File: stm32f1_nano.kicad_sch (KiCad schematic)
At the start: 50 parts, among them J1 Analog, J2 Digital, J3 TYPE-C-31-M-12, J4 Conn_ST_STDC14, J5 DEBUG, Q1 AO3401A, U1 STM32F103C8T6, U2 W25Q128JVSIQ, U3 AMS1117-3.3, U4 XC6206P332MR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

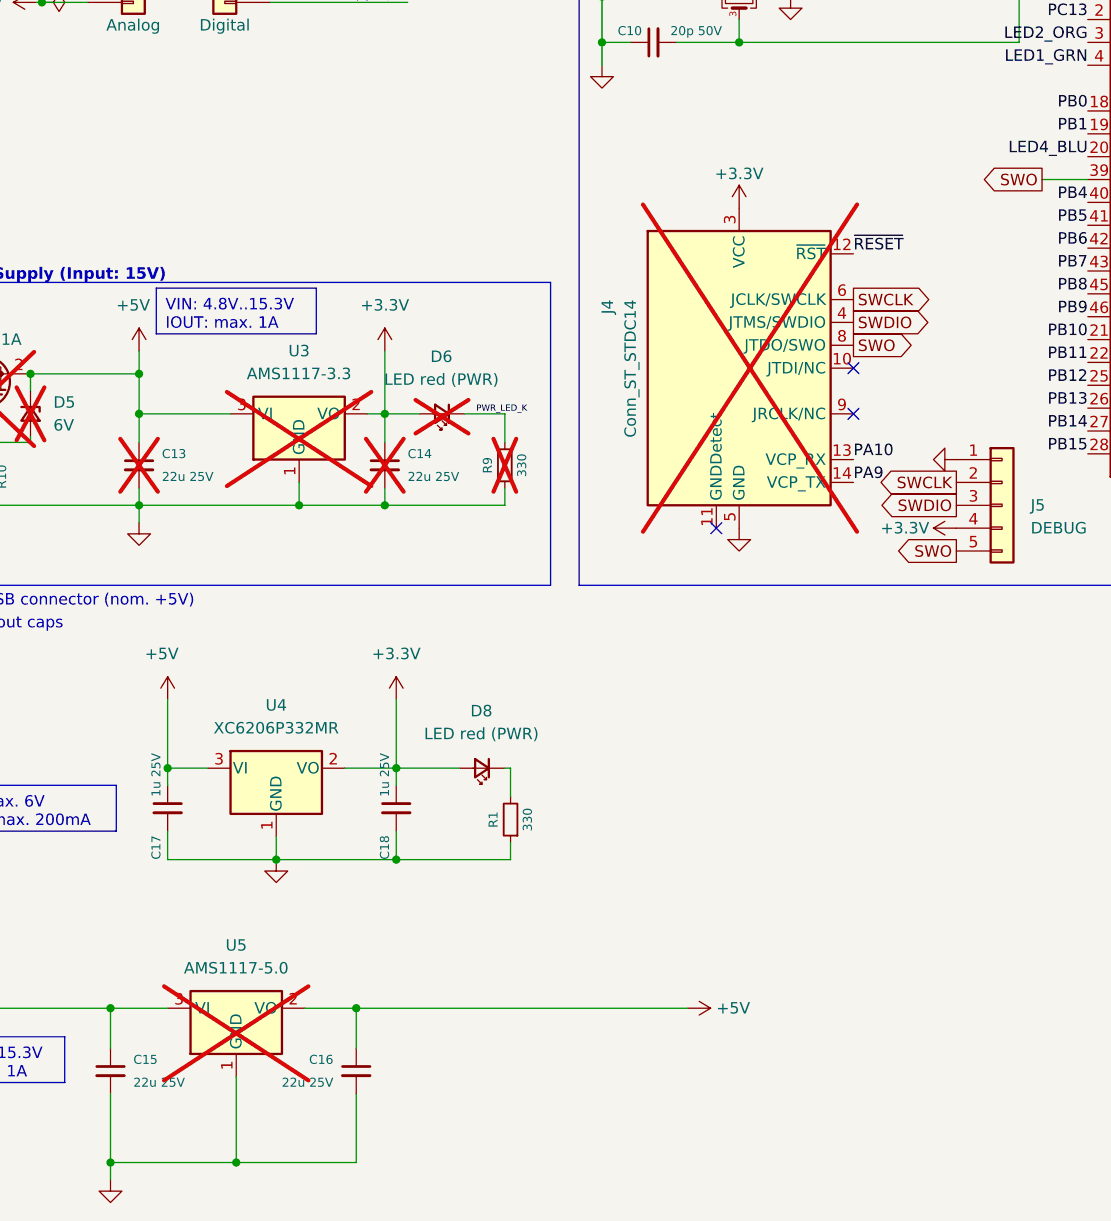
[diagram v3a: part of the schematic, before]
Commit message: #11 Use new central library KiCad-Lib
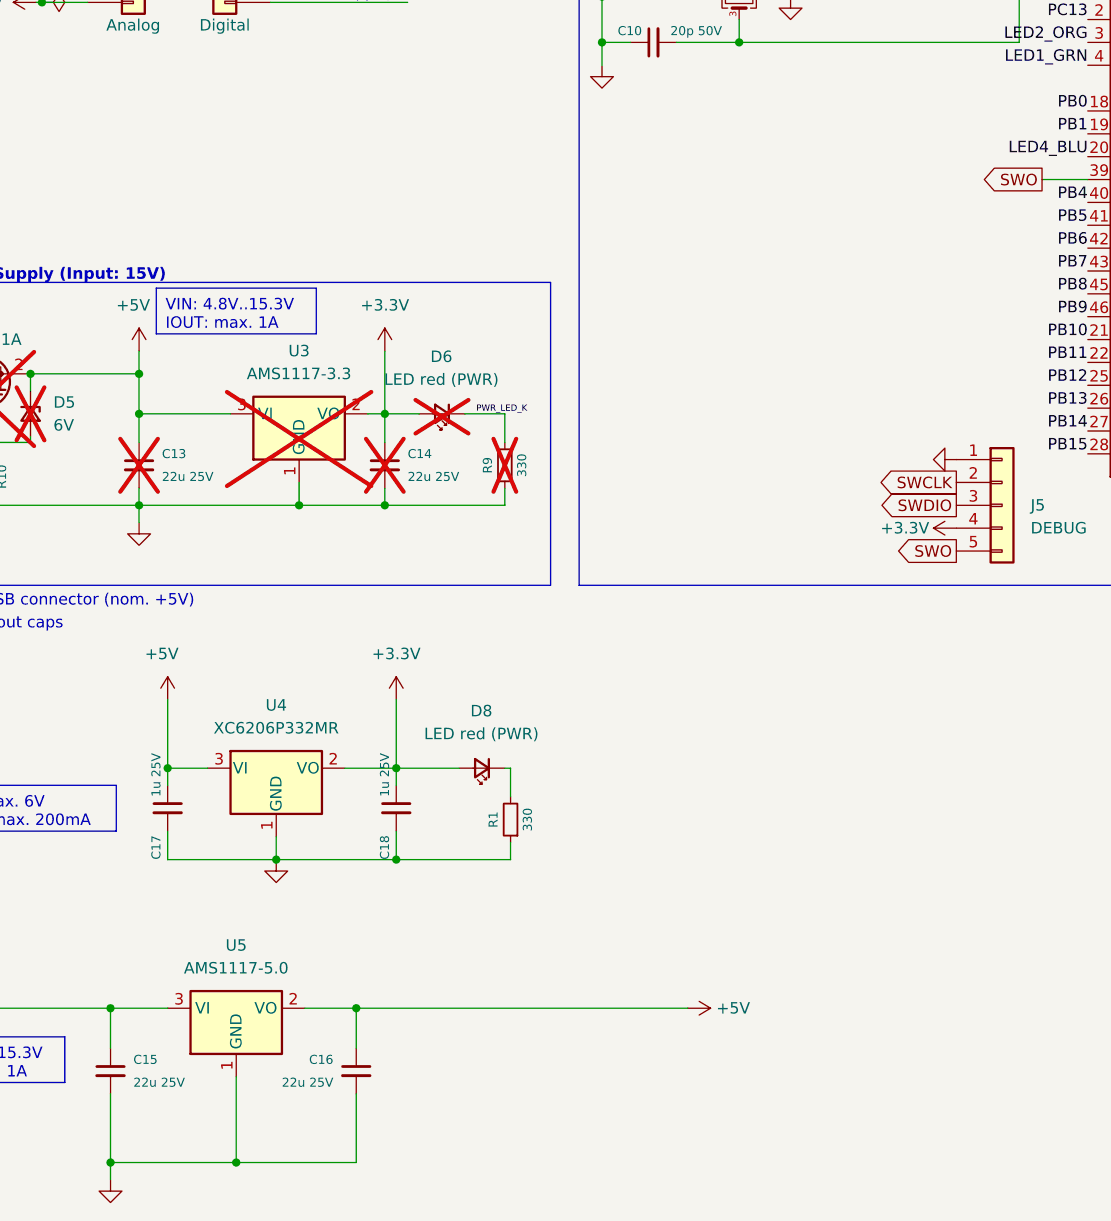
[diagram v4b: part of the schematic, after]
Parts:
- removed J4: Conn_ST_STDC14, Project_Library:Samtec_FTSH-107-XX-YYY-DV-K-A, symbol Connector:Conn_ST_STDC14
- U5: now fitted
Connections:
- no-connect marks 7 -> 4
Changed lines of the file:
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@@
   )
   (no_connect (at 35.56 31.75))
-  (no_connect (at 120.65 102.87))
-  (no_connect (at 120.65 107.95))
   (no_connect (at 236.22 111.76))
   (no_connect (at 55.88 57.15))
-  (no_connect (at 105.41 120.65))
   (no_connect (at 236.22 109.22))
   (wire (pts (xy 55.88 59.69) (xy 71.12 59.69))
@@
     (effects (font (size 1.27 1.27)) (justify right bottom))
   )
-  (label "PA10" (at 120.65 113.03 0) (fields_autoplaced)
-    (effects (font (size 1.27 1.27)) (justify left bottom))
-  )
   (label "PB14" (at 146.685 109.855 180) (fields_autoplaced)
     (effects (font (size 1.27 1.27)) (justify right bottom))
@@
     (effects (font (size 1.27 1.27)) (justify left bottom))
   )
-  (label "PA9" (at 120.65 115.57 0) (fields_autoplaced)
-    (effects (font (size 1.27 1.27)) (justify left bottom))
-  )
   (label "SPI1_MOSI" (at 179.705 92.075 0) (fields_autoplaced)
     (effects (font (size 1.27 1.27)) (justify left bottom))
@@
     (effects (font (size 1.27 1.27)) (justify left bottom))
   )
-  (label "~{RESET}" (at 120.65 90.17 0) (fields_autoplaced)
-    (effects (font (size 1.27 1.27)) (justify left bottom))
-  )
   (global_label "SWO" (shape output) (at 132.08 123.19 180) (fields_autoplaced)
     (effects (font (size 1.27 1.27)) (justify right))
@@
     )
   )
-  (global_label "SWDIO" (shape output) (at 120.65 97.79 0) (fields_autoplaced)
-    (effects (font (size 1.27 1.27)) (justify left))
-    (property "Intersheetrefs" "${INTERSHEET_REFS}" (at 128.9293 97.8694 0)
-      (effects (font (size 1.27 1.27)) (justify left) hide)
-    )
-  )
   (global_label "SWO" (shape output) (at 141.605 81.915 180) (fields_autoplaced)
     (effects (font (size 1.27 1.27)) (justify right))
@@
     )
   )
-  (global_label "SWO" (shape output) (at 120.65 100.33 0) (fields_autoplaced)
-    (effects (font (size 1.27 1.27)) (justify left))
-    (property "Intersheetrefs" "${INTERSHEET_REFS}" (at 127.0545 100.2506 0)
-      (effects (font (size 1.27 1.27)) (justify left) hide)
-    )
-  )
-  (global_label "SWCLK" (shape output) (at 120.65 95.25 0) (fields_autoplaced)
-    (effects (font (size 1.27 1.27)) (justify left))
-    (property "Intersheetrefs" "${INTERSHEET_REFS}" (at 129.2921 95.3294 0)
-      (effects (font (size 1.27 1.27)) (justify left) hide)
-    )
-  )
   (symbol (lib_id "Connector_Generic:Conn_01x15") (at 40.64 44.45 0) (unit 1)
     (in_bom no) (on_board yes) (dnp no)
@@
   )
   (symbol (lib_id "Device:C_Small") (at 201.93 80.01 180) (unit 1)
-    (in_bom no) (on_board no) (dnp yes)
+    (in_bom no) (on_board yes) (dnp yes)
     (property "Reference" "C12" (at 200.66 75.565 90)
       (effects (font (size 1 1)) (justify left))
@@
   )
   (symbol (lib_id "Memory_Flash:W25Q32JVSS") (at 212.725 66.04 0) (unit 1)
-    (in_bom no) (on_board no) (dnp yes) (fields_autoplaced)
+    (in_bom no) (on_board yes) (dnp yes) (fields_autoplaced)
     (property "Reference" "U2" (at 221.615 64.77 0)
       (effects (font (size 1.27 1.27)) (justify left))
@@
     )
   )
-  (symbol (lib_id "power:+3.3V") (at 107.95 85.09 0) (unit 1)
-    (in_bom yes) (on_board yes) (dnp no)
-    (property "Reference" "#PWR020" (at 107.95 88.9 0)
-      (effects (font (size 1.27 1.27)) hide)
-    )
-    (property "Value" "+3.3V" (at 107.95 81.28 0)
-      (effects (font (size 1.27 1.27)))
-    )
-    (property "Footprint" "" (at 107.95 85.09 0)
-      (effects (font (size 1.27 1.27)) hide)
-    )
-    (property "Datasheet" "" (at 107.95 85.09 0)
-      (effects (font (size 1.27 1.27)) hide)
-    )
-    (pin "1")
-    (instances
-      (project "stm32f1_nano"
-        (path "/0d35483a-0b12-46cc-b9f2-896fd6831779"
-          (reference "#PWR020") (unit 1)
-        )
-      )
-      (project "stm32f1"
-        (path "/5e832605-8ffe-4662-837d-abaa536d3f2c"
-          (reference "#PWR015") (unit 1)
-        )
-      )
-    )
-  )
   (symbol (lib_id "Device:R_Small") (at 238.125 34.29 180) (unit 1)
     (in_bom yes) (on_board yes) (dnp no)
@@
   )
   (symbol (lib_id "Regulator_Linear:AMS1117-3.3") (at 52.07 173.99 0) (unit 1)
-    (in_bom yes) (on_board no) (dnp yes) (fields_autoplaced)
+    (in_bom yes) (on_board yes) (dnp no) (fields_autoplaced)
     (property "Reference" "U5" (at 52.07 167.005 0)
       (effects (font (size 1.27 1.27)))
@@
     )
   )
-  (symbol (lib_id "power:GND") (at 107.95 120.65 0) (unit 1)
-    (in_bom yes) (on_board yes) (dnp no) (fields_autoplaced)
-    (property "Reference" "#PWR027" (at 107.95 127 0)
-      (effects (font (size 1.27 1.27)) hide)
-    )
-    (property "Value" "GND" (at 107.95 125.73 0)
-      (effects (font (size 1.27 1.27)) hide)
-    )
-    (property "Footprint" "" (at 107.95 120.65 0)
-      (effects (font (size 1.27 1.27)) hide)
-    )
-    (property "Datasheet" "" (at 107.95 120.65 0)
-      (effects (font (size 1.27 1.27)) hide)
-    )
-    (pin "1")
-    (instances
-      (project "stm32f1_nano"
-        (path "/0d35483a-0b12-46cc-b9f2-896fd6831779"
-          (reference "#PWR027") (unit 1)
-        )
-      )
-      (project "debugboard"
-        (path "/c4be5c82-3834-4d46-ac8c-ca62cb8b7a5a"
-          (reference "#PWR0106") (unit 1)
-        )
-      )
-    )
-  )
   (symbol (lib_id "power:+5V") (at 222.885 81.28 90) (unit 1)
     (in_bom yes) (on_board yes) (dnp no)
@@
         )
       )
-    )
-  )
-  (symbol (lib_id "Connector:Conn_ST_STDC14") (at 107.95 102.87 0) (unit 1)
-    (in_bom no) (on_board no) (dnp yes)
-    (property "Reference" "J4" (at 93.345 95.25 90)
-      (effects (font (size 1.27 1.27)) (justify right))
-    )
-    (property "Value" "Conn_ST_STDC14" (at 95.885 95.25 90)
-      (effects (font (size 1.27 1.27)) (justify right))
-    )
-    (property "Footprint" "Project_Library:Samtec_FTSH-107-XX-YYY-DV-K-A" (at 107.95 102.87 0)
-      (effects (font (size 1.27 1.27)) hide)
-    )
-    (property "Datasheet" "https://www.st.com/content/ccc/resource/technical/document/user_manual/group1/99/49/91/b6/b2/3a/46/e5/DM00526767/files/DM00526767.pdf/jcr:content/translations/en.DM00526767.pdf" (at 99.06 134.62 90)
-      (effects (font (size 1.27 1.27)) hide)
-    )
-    (property "Manufacturer" "Samtec" (at 107.95 102.87 0)
-      (effects (font (size 1.27 1.27)) hide)
-    )
-    (property "Partnumber" "FTSH-107-01-L-DV-K-A" (at 107.95 102.87 0)
-      (effects (font (size 1.27 1.27)) hide)
-    )
-    (property "Description" "" (at 107.95 102.87 0)
-      (effects (font (size 1.27 1.27)) hide)
-    )
-    (property "JLCPCB Part #" "" (at 107.95 102.87 0)
-      (effects (font (size 1.27 1.27)) hide)
-    )
-    (property "isBasicPart" "" (at 107.95 102.87 0)
-      (effects (font (size 1.27 1.27)) hide)
-    )
-    (property "Description" "" (at 107.95 102.87 0)
-      (effects (font (size 1.27 1.27)) hide)
-    )
-    (property "JLCPCB Part #" "" (at 107.95 102.87 0)
-      (effects (font (size 1.27 1.27)) hide)
-    )
-    (property "isBasicPart" "" (at 107.95 102.87 0)
-      (effects (font (size 1.27 1.27)) hide)
-    )
-    (pin "1")
-    (pin "10")
-    (pin "11")
-    (pin "12")
-    (pin "13")
-    (pin "14")
-    (pin "2")
-    (pin "3")
-    (pin "4")
-    (pin "5")
-    (pin "6")
-    (pin "7")
-    (pin "8")
-    (pin "9")
-    (instances
-      (project "stm32f1_nano"
-        (path "/0d35483a-0b12-46cc-b9f2-896fd6831779"
-          (reference "J4") (unit 1)
-        )
-      )
-      (project "debugboard"
-        (path "/c4be5c82-3834-4d46-ac8c-ca62cb8b7a5a"
-          (reference "J1") (unit 1)
-        )
-      )

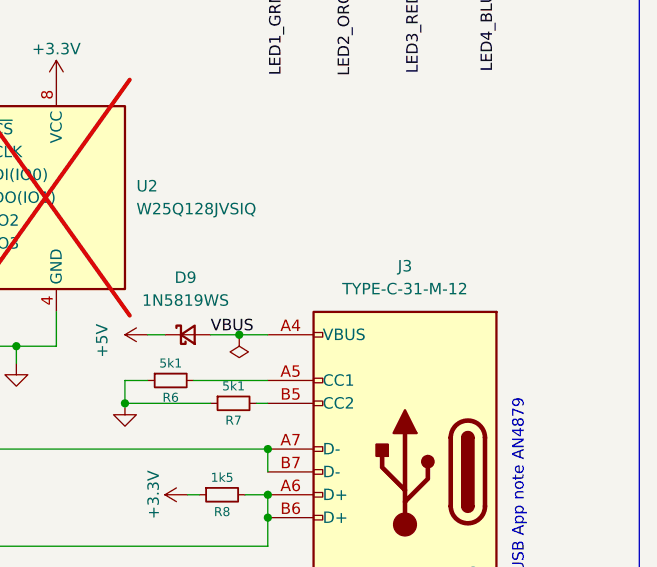
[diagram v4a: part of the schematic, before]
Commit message: #10 Change USB connector to SHOU HAN TYPE-C 16PIN 2MD(073) (C2765186)
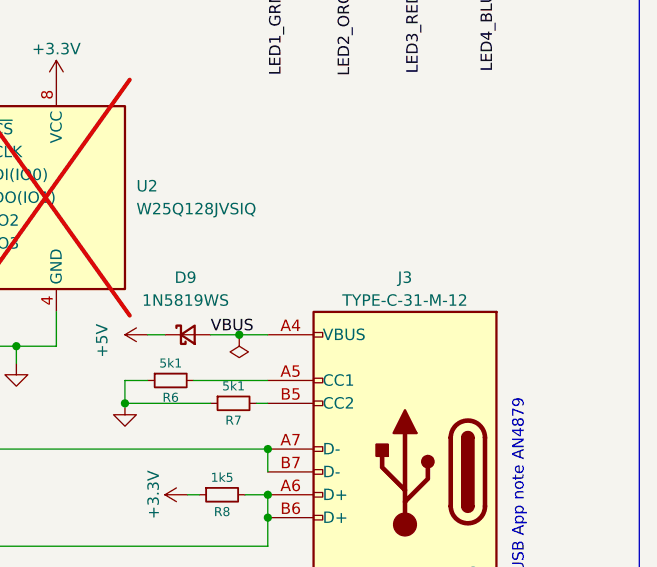
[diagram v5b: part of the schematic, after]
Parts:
- J3: footprint Connector_USB:USB_C_Receptacle_HRO_TYPE-C-31-M-12 -> #Connector:SHOU HAN TYPE-C 16PIN 2MD(073); symbol Project_Library:USB_C_Receptacle_USB2.0 -> #Connector:SHOU HAN TYPE-C 16PIN 2MD(073); JLCPCB Part # C165948 -> C2765186; Manufacturer Korean Hroparts Elec -> SHOU HAN; Partnumber TYPE-C-31-M-12 -> TYPE-C 16PIN 2MD(073)
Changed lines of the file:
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@@
     )
   )
-  (symbol (lib_id "Project_Library:USB_C_Receptacle_USB2.0") (at 251.46 96.52 0) (mirror y) (unit 1)
-    (in_bom yes) (on_board yes) (dnp no) (fields_autoplaced)
-    (property "Reference" "J3" (at 251.46 73.66 0)
+  (symbol (lib_id "#Connector:SHOU HAN TYPE-C 16PIN 2MD(073)") (at 251.46 96.52 0) (mirror y) (unit 1)
+    (in_bom yes) (on_board yes) (dnp no)
+    (property "Reference" "J3" (at 251.46 74.93 0)
       (effects (font (size 1.27 1.27)))
     )
-    (property "Value" "TYPE-C-31-M-12" (at 251.46 76.2 0)
+    (property "Value" "TYPE-C-31-M-12" (at 251.46 77.47 0)
       (effects (font (size 1.27 1.27)))
     )
-    (property "Footprint" "Connector_USB:USB_C_Receptacle_HRO_TYPE-C-31-M-12" (at 250.952 129.032 0)
+    (property "Footprint" "#Connector:SHOU HAN TYPE-C 16PIN 2MD(073)" (at 250.952 129.032 0)
       (effects (font (size 1.27 1.27)) hide)
     )
-    (property "Datasheet" "https://www.usb.org/sites/default/files/documents/usb_type-c.zip" (at 252.984 126.746 0)
+    (property "Datasheet" "${KIPRJMOD}/KiCad-Lib/#Connector.doc/SHOU HAN TYPE-C 16PIN 2MD(073).pdf" (at 252.984 126.746 0)
       (effects (font (size 1.27 1.27)) hide)
     )
@@
       (effects (font (size 1.27 1.27)) hide)
     )
-    (property "Description" "5A 1 16 Female Type-C SMD  USB Connectors ROHS" (at 251.46 96.52 0)
+    (property "Description" "5A 1 Surface Mount 16P Female -25℃~+85℃ Type-C SMD USB Connectors ROHS" (at 251.46 134.62 0)
       (effects (font (size 1.27 1.27)) hide)
     )
-    (property "Manufacturer" "Korean Hroparts Elec" (at 251.46 96.52 0)
+    (property "Manufacturer" "SHOU HAN" (at 251.46 137.16 0)
       (effects (font (size 1.27 1.27)) hide)
     )
-    (property "Partnumber" "TYPE-C-31-M-12" (at 251.46 96.52 0)
+    (property "Partnumber" "TYPE-C 16PIN 2MD(073)" (at 251.46 139.7 0)
       (effects (font (size 1.27 1.27)) hide)
     )
-    (property "JLCPCB Part #" "C165948" (at 251.46 96.52 0)
+    (property "JLCPCB Part #" "C2765186" (at 251.46 132.08 0) (show_name)
       (effects (font (size 1.27 1.27)) hide)
     )
@@
       (effects (font (size 1.27 1.27)) hide)
     )
-    (property "isBasicPart" "NO" (at 251.46 96.52 0)
+    (property "isBasicPart" "NO" (at 251.46 142.24 0) (show_name)
       (effects (font (size 1.27 1.27)) hide)
     )
